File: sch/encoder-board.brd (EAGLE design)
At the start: 18.8 x 17.1 mm, 2 parts

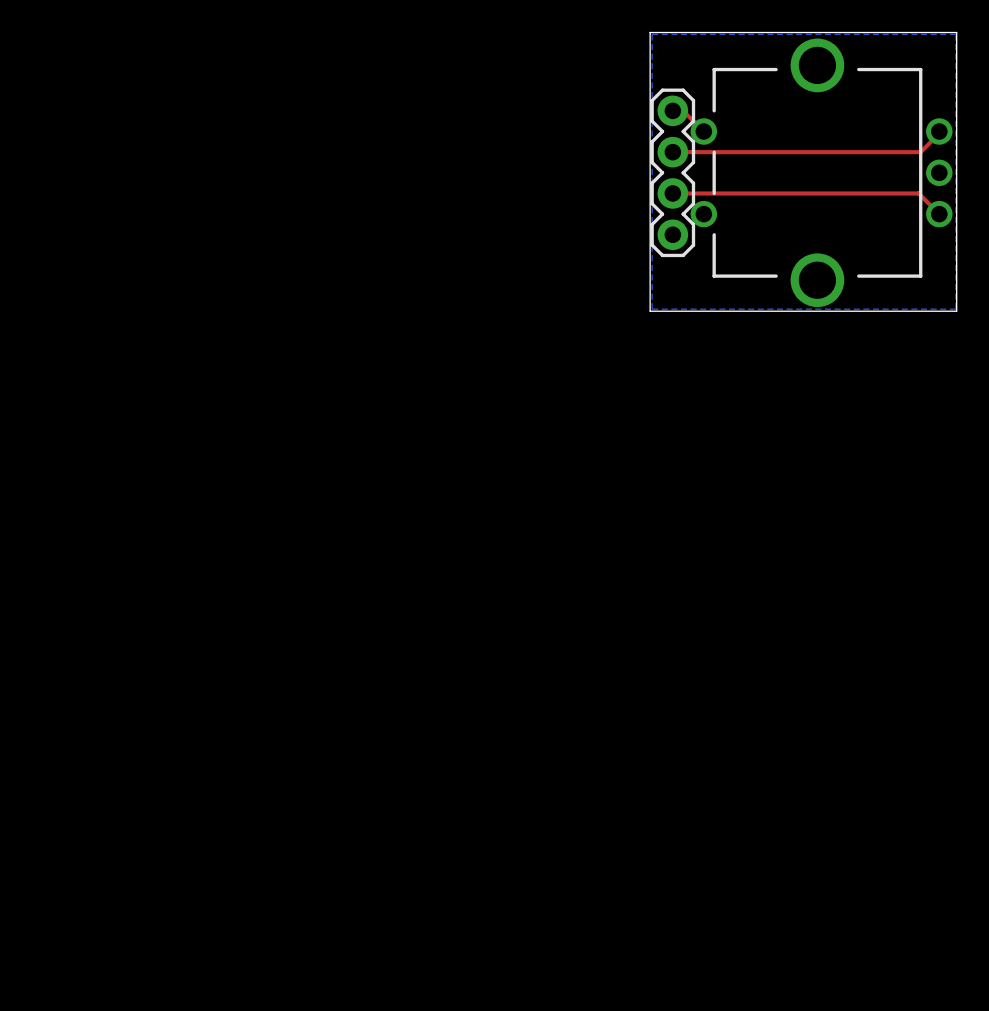
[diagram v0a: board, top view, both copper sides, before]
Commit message: refactoring: added vcc pour, updated capacitors footprints fix: correct orientation of 7segment displays
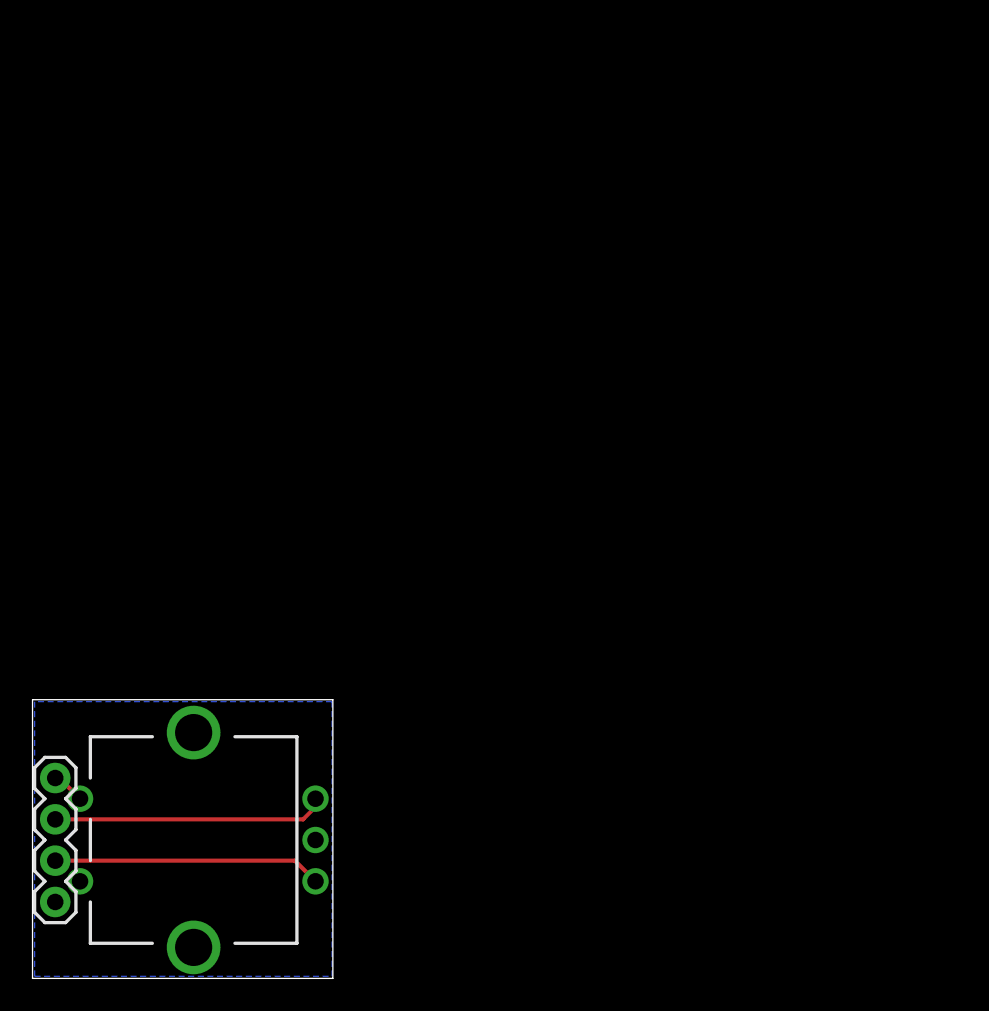
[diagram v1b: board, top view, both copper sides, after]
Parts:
- moved S1 56.2 mm to (9.91, 8.51)
- moved J1 55.9 mm to (1.40, 4.70)
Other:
- board size 18.8 x 17.1 mm -> 18.5 x 17.1 mm
- board text removed: "E1"
- board text removed: "E2"
- board text removed: "GND"
- board text removed: "SW"
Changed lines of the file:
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@@
 <board>
 <plain>
-<wire x1="37.973" y1="41.021" x2="56.82" y2="41.021" width="0" layer="20"/>
-<wire x1="56.82" y1="41.021" x2="56.82" y2="58.156" width="0" layer="20"/>
-<wire x1="56.82" y1="58.156" x2="37.973" y2="58.156" width="0" layer="20"/>
-<wire x1="37.973" y1="58.156" x2="37.973" y2="41.021" width="0" layer="20"/>
-<text x="40.64" y="54.229" size="1.016" layer="26" align="top-left">SW</text>
-<text x="40.64" y="49.911" size="1.016" layer="26">E1</text>
-<text x="40.64" y="49.149" size="1.016" layer="26" align="top-left">E2</text>
-<text x="40.64" y="44.831" size="1.016" layer="26">GND</text>
+<wire x1="0" y1="0" x2="18.466" y2="0" width="0" layer="20"/>
+<wire x1="18.466" y1="0" x2="18.466" y2="17.135" width="0" layer="20"/>
+<wire x1="18.466" y1="17.135" x2="0" y2="17.135" width="0" layer="20"/>
+<wire x1="0" y1="17.135" x2="0" y2="0" width="0" layer="20"/>
+<text x="3.175" y="12.7" size="0.508" layer="25" rot="R270" align="center"></text>
+<text x="3.175" y="9.271" size="0.508" layer="25" rot="R270" align="center"></text>
+<text x="3.175" y="7.874" size="0.508" layer="25" rot="R270" align="center"></text>
+<text x="3.175" y="3.937" size="0.508" layer="25" rot="R270" align="center"></text>
 </plain>
 <attributes>
@@
 </autorouter>
 <elements>
-<element name="S1" library="SparkFun-Switches" library_urn="urn:adsk.eagle:library:535" package="ROTARY_ENC_PLAIN" package3d_urn="urn:adsk.eagle:package:40158/1" value="ENCODER-SWITCH" x="48.26" y="49.53" smashed="yes">
-<attribute name="SF_SKU" value="COM-09117" x="48.26" y="49.53" size="1.778" layer="27" display="off"/>
+<element name="S1" library="SparkFun-Switches" library_urn="urn:adsk.eagle:library:535" package="ROTARY_ENC_PLAIN" package3d_urn="urn:adsk.eagle:package:40158/1" value="ENCODER-SWITCH" x="9.906" y="8.509" smashed="yes">
+<attribute name="SF_SKU" value="COM-09117" x="9.906" y="8.509" size="1.778" layer="27" display="off"/>
 </element>
-<element name="J1" library="SparkFun-Connectors" library_urn="urn:adsk.eagle:library:513" package="1X04" package3d_urn="urn:adsk.eagle:package:38085/1" value="" x="39.37" y="45.72" smashed="yes" rot="R90">
-<attribute name="PROD_ID" value="CONN-09696" x="39.37" y="45.72" size="1.778" layer="27" rot="R90" display="off"/>
-<attribute name="VALUE" x="41.402" y="44.45" size="0.6096" layer="27" font="vector" ratio="20" rot="R90"/>
+<element name="J1" library="SparkFun-Connectors" library_urn="urn:adsk.eagle:library:513" package="1X04" package3d_urn="urn:adsk.eagle:package:38085/1" value="" x="1.397" y="4.699" smashed="yes" rot="R90">
+<attribute name="PROD_ID" value="CONN-09696" x="1.397" y="4.699" size="1.778" layer="27" rot="R90" display="off"/>
+<attribute name="VALUE" x="3.429" y="3.429" size="0.6096" layer="27" font="vector" ratio="20" rot="R90"/>
 </element>
 </elements>
@@
 <contactref element="S1" pad="B"/>
 <contactref element="J1" pad="3"/>
-<wire x1="39.37" y1="50.8" x2="54.61" y2="50.8" width="0.254" layer="1"/>
-<wire x1="54.61" y1="50.8" x2="55.753" y2="51.943" width="0.254" layer="1"/>
-<wire x1="55.753" y1="51.943" x2="55.753" y2="52.07" width="0.254" layer="1"/>
+<wire x1="1.397" y1="9.779" x2="16.637" y2="9.779" width="0.254" layer="1"/>
+<wire x1="16.637" y1="9.779" x2="17.399" y2="10.541" width="0.254" layer="1"/>
+<wire x1="17.399" y1="10.541" x2="17.399" y2="11.049" width="0.254" layer="1"/>
 </signal>
 <signal name="E2">
 <contactref element="S1" pad="A"/>
 <contactref element="J1" pad="2"/>
-<wire x1="39.37" y1="48.26" x2="54.483" y2="48.26" width="0.254" layer="1"/>
-<wire x1="54.483" y1="48.26" x2="55.753" y2="46.99" width="0.254" layer="1"/>
+<wire x1="1.397" y1="7.239" x2="16.129" y2="7.239" width="0.254" layer="1"/>
+<wire x1="16.129" y1="7.239" x2="17.399" y2="5.969" width="0.254" layer="1"/>
 </signal>
 <signal name="SW">
 <contactref element="J1" pad="4"/>
 <contactref element="S1" pad="SW+"/>
-<wire x1="39.37" y1="53.34" x2="40.005" y2="53.34" width="0.254" layer="1"/>
-<wire x1="40.005" y1="53.34" x2="41.275" y2="52.07" width="0.254" layer="1"/>
+<wire x1="1.397" y1="12.319" x2="1.651" y2="12.319" width="0.254" layer="1"/>
+<wire x1="1.651" y1="12.319" x2="2.921" y2="11.049" width="0.254" layer="1"/>
 </signal>
 <signal name="GND">
@@
 <contactref element="S1" pad="C"/>
 <polygon width="0.1524" layer="16">
-<vertex x="38.1" y="58.039"/>
-<vertex x="38.1" y="41.148"/>
-<vertex x="56.769" y="41.148"/>
-<vertex x="56.769" y="58.039"/>
+<vertex x="0.127" y="17.018"/>
+<vertex x="0.127" y="0.127"/>
+<vertex x="18.415" y="0.127"/>
+<vertex x="18.415" y="17.018"/>
 </polygon>
 </signal>
